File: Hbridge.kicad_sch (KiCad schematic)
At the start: 38 parts, among them J1 nodeLync IN, J2 nodeLync OUT, J3 Conn_02x05_Odd_Even, J4 Motor, J5 Power Pole, J6 Conn_02x02_Odd_Even, U1 MCP23008-E/P, U2 VNH7100BASTR, U3 MCP3427-E/UN

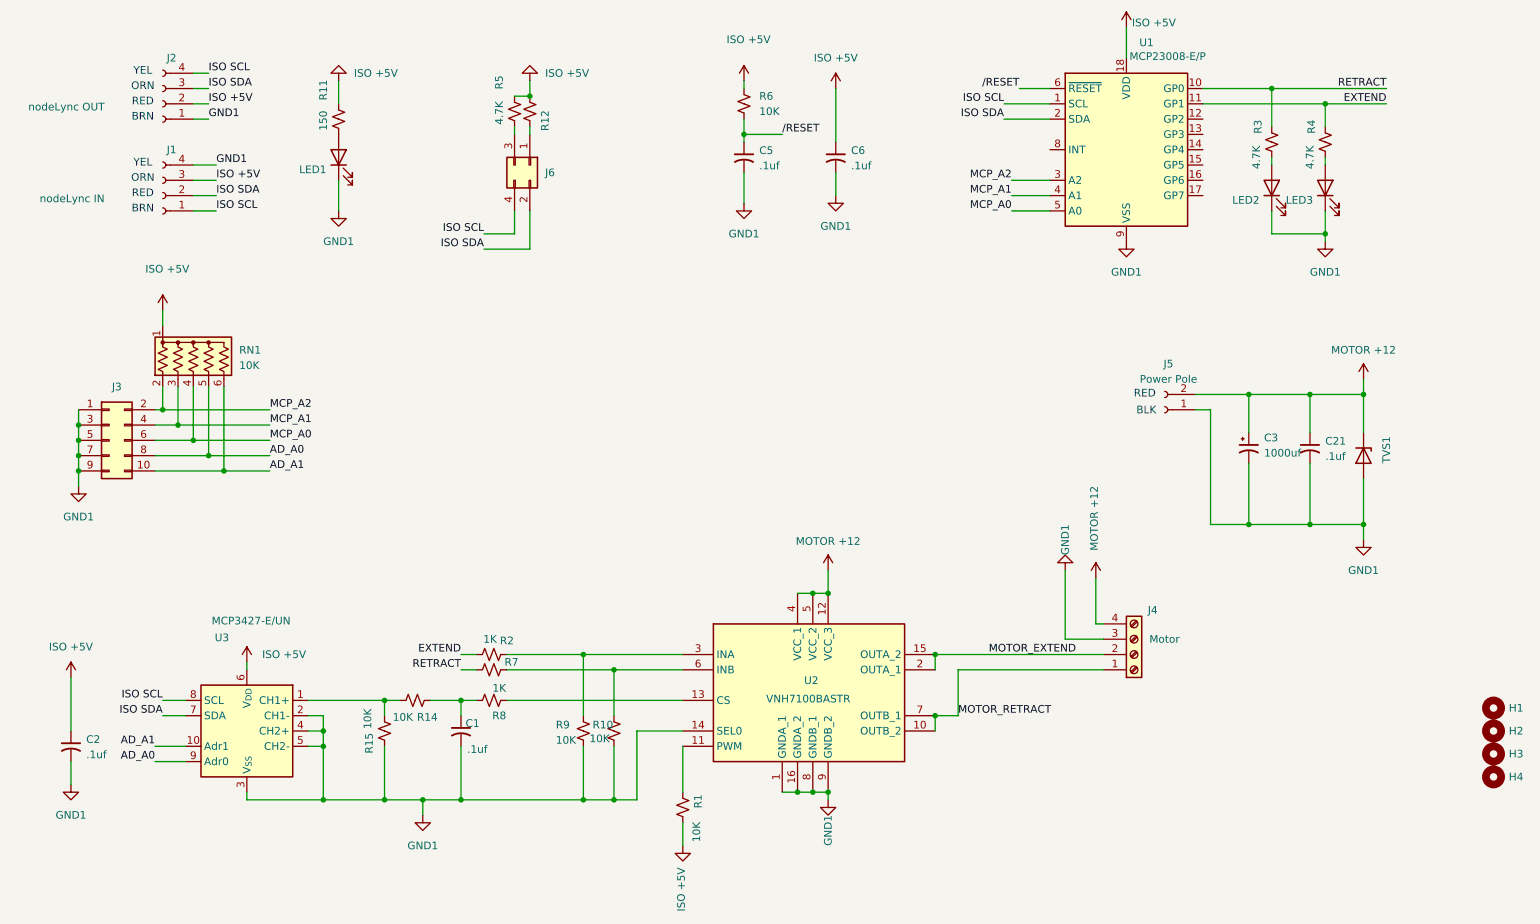
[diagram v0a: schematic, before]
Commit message: corrected issues with sense resistor for CS and SEL
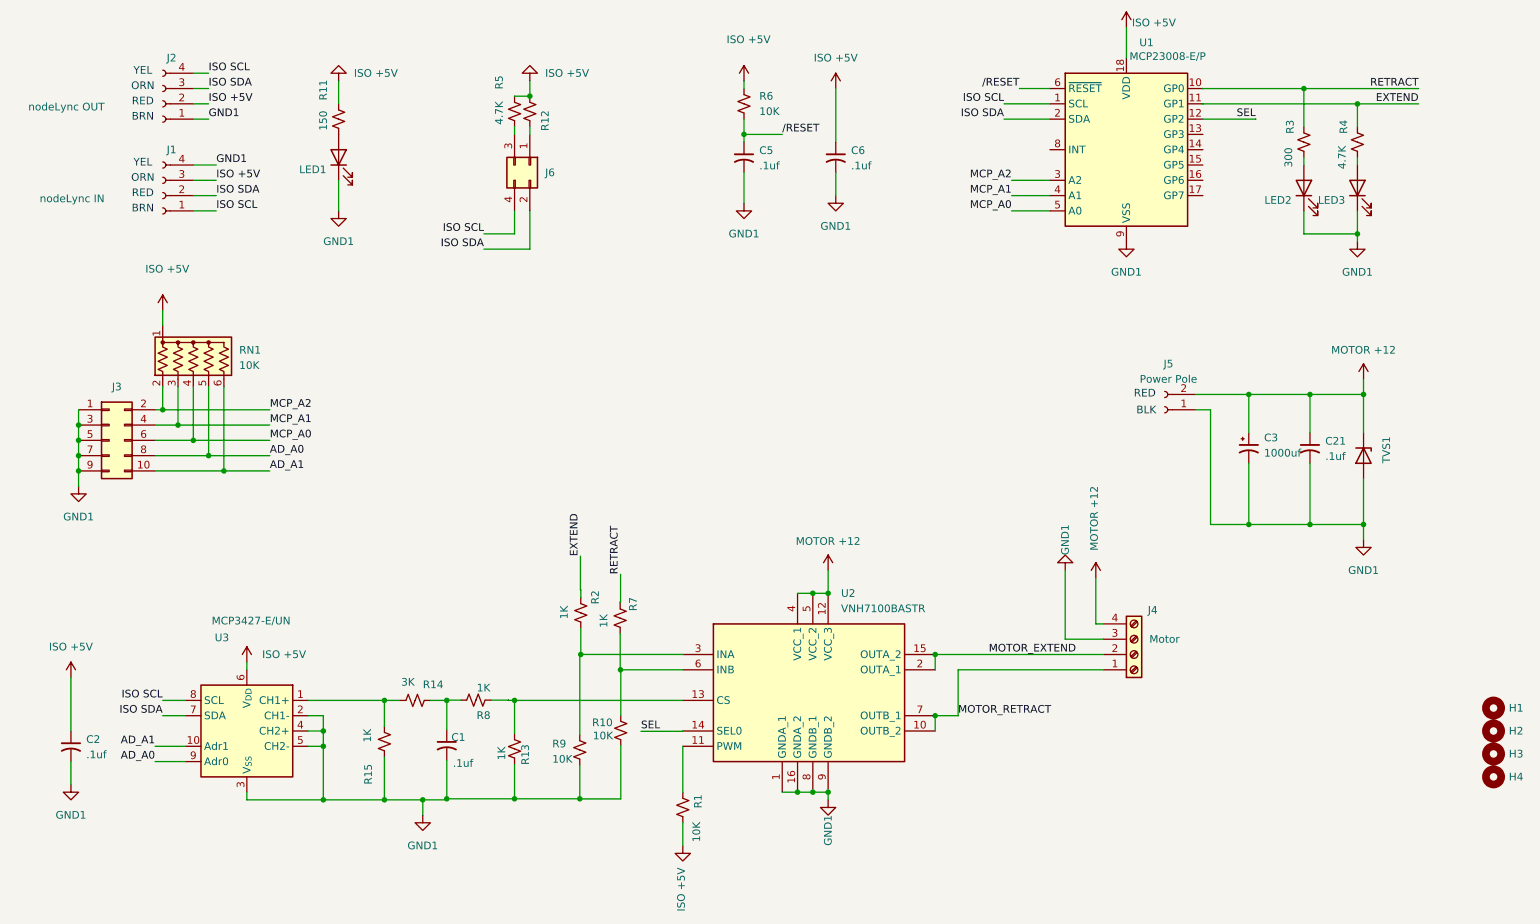
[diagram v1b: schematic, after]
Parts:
- added R13: 1K, Resistor_THT:R_Axial_DIN0204_L3.6mm_D1.6mm_P7.62mm_Horizontal, symbol Device:R_Small_US
- R14: value 10K -> 3K
- R15: value 10K -> 1K
- R3: value 4.7K -> 300
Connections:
- net EXTEND: now also R2.2; no longer R2.1
- net GND1: now also R13.1; no longer U2.14 (SEL0)
- net RETRACT: now also R7.2; no longer R7.1
- net at R10.1, U2.6 (INB): now also R7.1; no longer R7.2
- net SEL: now reaches U1.12 (GP2)
- net SEL: now also U2.14 (SEL0)
- net at R9.1, U2.3 (INA): now also R2.1; no longer R2.2
- net at R8.2, U2.13 (CS): now also R13.2
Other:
- moved on the sheet: C1, LED2, LED3, R10, R15, R2, R3, R4, R7, R8, R9
